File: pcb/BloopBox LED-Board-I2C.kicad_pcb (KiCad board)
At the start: 4 copper layers, 25 x 41.5 mm, 20 parts, among them J1 I2C, J2 V_BM, U1 IS31FL3199

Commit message: fix: add part numbers
Add missing LSCS Part numbers
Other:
- board text added: "BloopBox LED-Board I2C"
- board text removed: "BloopBox LED-Board"
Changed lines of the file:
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@@
     (descr "Capacitor SMD 0402 (1005 Metric), square (rectangular) end terminal, IPC_7351 nominal, (Body size source: IPC-SM-782 page 76, https://www.pcb-3d.com/wordpress/wp-content/uploads/ipc-sm-782a_amendment_1_and_2.pdf), generated with kicad-footprint-generator")
     (tags "capacitor")
+    (property "LCSC" "C52923")
     (property "Sheetfile" "BloopBox LED-Board-I2C.kicad_sch")
     (property "Sheetname" "")
@@
       (rotate (xyz 0 0 0))
     )
+    (model "${KICAD6_3DMODEL_DIR}/Package_DFN_QFN.3dshapes/QFN-20-1EP_3x3mm_P0.45mm_EP1.6x1.6mm.wrl"
+      (offset (xyz 0 0 0))
+      (scale (xyz 1 1 1))
+      (rotate (xyz 0 0 0))
+    )
   )
   (footprint "My_Footprints:JLCPCB_Tooling_Hole" (layer "F.Cu")
@@
     (descr "Capacitor SMD 0402 (1005 Metric), square (rectangular) end terminal, IPC_7351 nominal, (Body size source: IPC-SM-782 page 76, https://www.pcb-3d.com/wordpress/wp-content/uploads/ipc-sm-782a_amendment_1_and_2.pdf), generated with kicad-footprint-generator")
     (tags "capacitor")
+    (property "LCSC" "C1525")
     (property "Sheetfile" "BloopBox LED-Board-I2C.kicad_sch")
     (property "Sheetname" "")
@@
     (descr "Capacitor SMD 0402 (1005 Metric), square (rectangular) end terminal, IPC_7351 nominal, (Body size source: IPC-SM-782 page 76, https://www.pcb-3d.com/wordpress/wp-content/uploads/ipc-sm-782a_amendment_1_and_2.pdf), generated with kicad-footprint-generator")
     (tags "capacitor")
+    (property "LCSC" "C1525")
     (property "Sheetfile" "BloopBox LED-Board-I2C.kicad_sch")
     (property "Sheetname" "")
@@
     (descr "Resistor SMD 0402 (1005 Metric), square (rectangular) end terminal, IPC_7351 nominal, (Body size source: IPC-SM-782 page 72, https://www.pcb-3d.com/wordpress/wp-content/uploads/ipc-sm-782a_amendment_1_and_2.pdf), generated with kicad-footprint-generator")
     (tags "resistor")
+    (property "LCSC" "C25741")
     (property "Sheetfile" "BloopBox LED-Board-I2C.kicad_sch")
     (property "Sheetname" "")
@@
     (effects (font (size 1 1) (thickness 0.15)) (justify mirror))
   )
-  (gr_text "BloopBox\nLED-Board" (at 142.75 105.25) (layer "B.SilkS")
+  (gr_text "BloopBox\nLED-Board\nI2C" (at 142.75 107) (layer "B.SilkS")
     (effects (font (size 1.2 1.2) (thickness 0.2)) (justify mirror))
   )

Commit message: fix: add pin description
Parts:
- moved G*** 1.00 mm to (157.2, 106.0)
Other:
- board text added: "+"
- board text added: "-"
- board text added: "SCL"
- board text added: "SDA"
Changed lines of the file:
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@@
   )
   (footprint "My_Footprints:CutieMark5mmInverted" (layer "B.Cu")
-    (at 157.25 107 180)
+    (at 157.25 106 180)
     (attr board_only exclude_from_pos_files exclude_from_bom)
     (fp_text reference "G***" (at 0 0) (layer "B.SilkS") hide
@@
   (gr_line (start 137.5 85.5) (end 146.5 85.5) (layer "Edge.Cuts") (width 0.1))
   (gr_arc (start 142.5 115) (mid 138.964466 113.535534) (end 137.5 110) (layer "Edge.Cuts") (width 0.1))
-  (gr_text "qete.sh/el" (at 157.25 110.5) (layer "B.SilkS")
+  (gr_text "-" (at 153 111.75) (layer "B.SilkS")
+    (effects (font (size 1 1) (thickness 0.15)) (justify mirror))
+  )
+  (gr_text "qete.sh/el" (at 157.25 109.5) (layer "B.SilkS")
+    (effects (font (size 1 1) (thickness 0.15)) (justify mirror))
+  )
+  (gr_text "SDA" (at 149.25 111.75) (layer "B.SilkS")
+    (effects (font (size 1 0.75) (thickness 0.15)) (justify mirror))
+  )
+  (gr_text "+" (at 151 111.75) (layer "B.SilkS")
     (effects (font (size 1 1) (thickness 0.15)) (justify mirror))
   )
@@
     (effects (font (size 1.2 1.2) (thickness 0.2)) (justify mirror))
   )
+  (gr_text "SCL" (at 147 111.75) (layer "B.SilkS")
+    (effects (font (size 1 0.75) (thickness 0.15)) (justify mirror))
+  )
   (gr_text "JLCJLCJLCJLC" (at 158 121.25) (layer "F.SilkS")

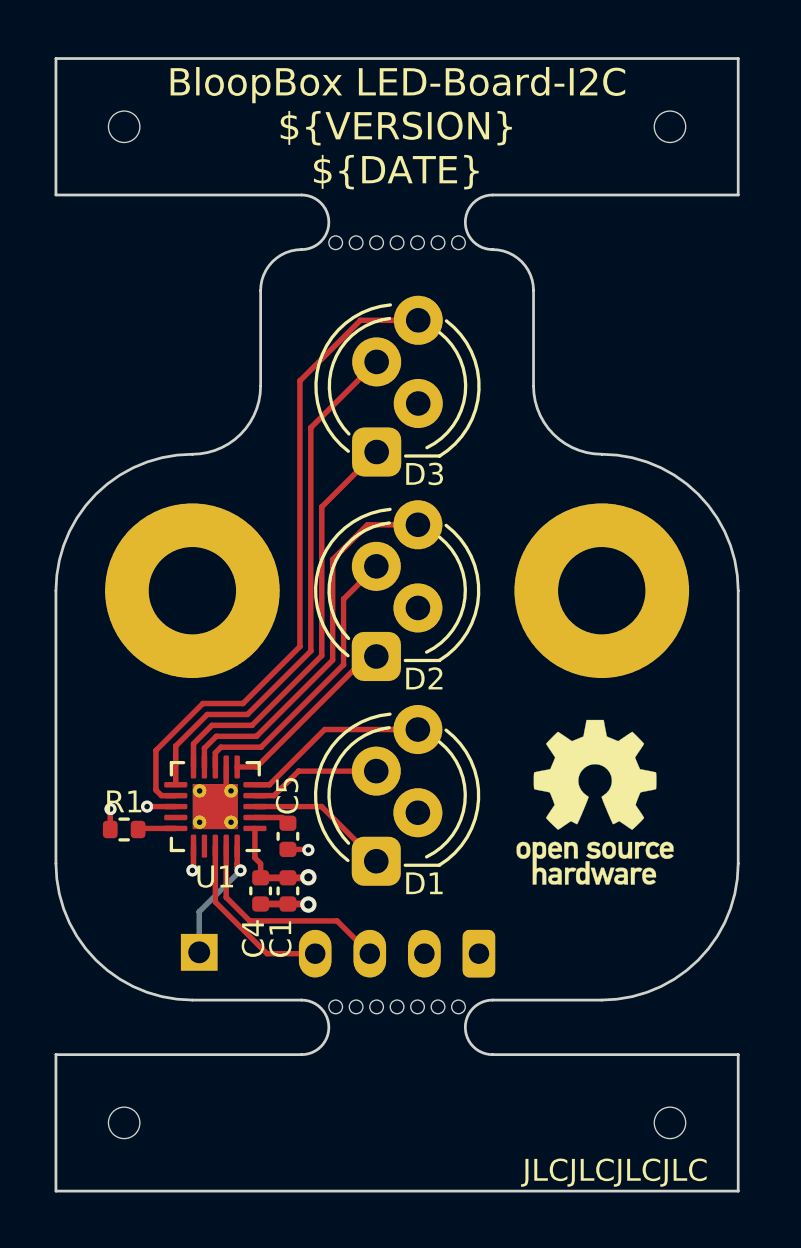
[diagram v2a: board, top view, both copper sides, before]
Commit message: feat: change LED controller to AW2013
replace the IS31FL3199 with AW2013 and remove additional LED footprints
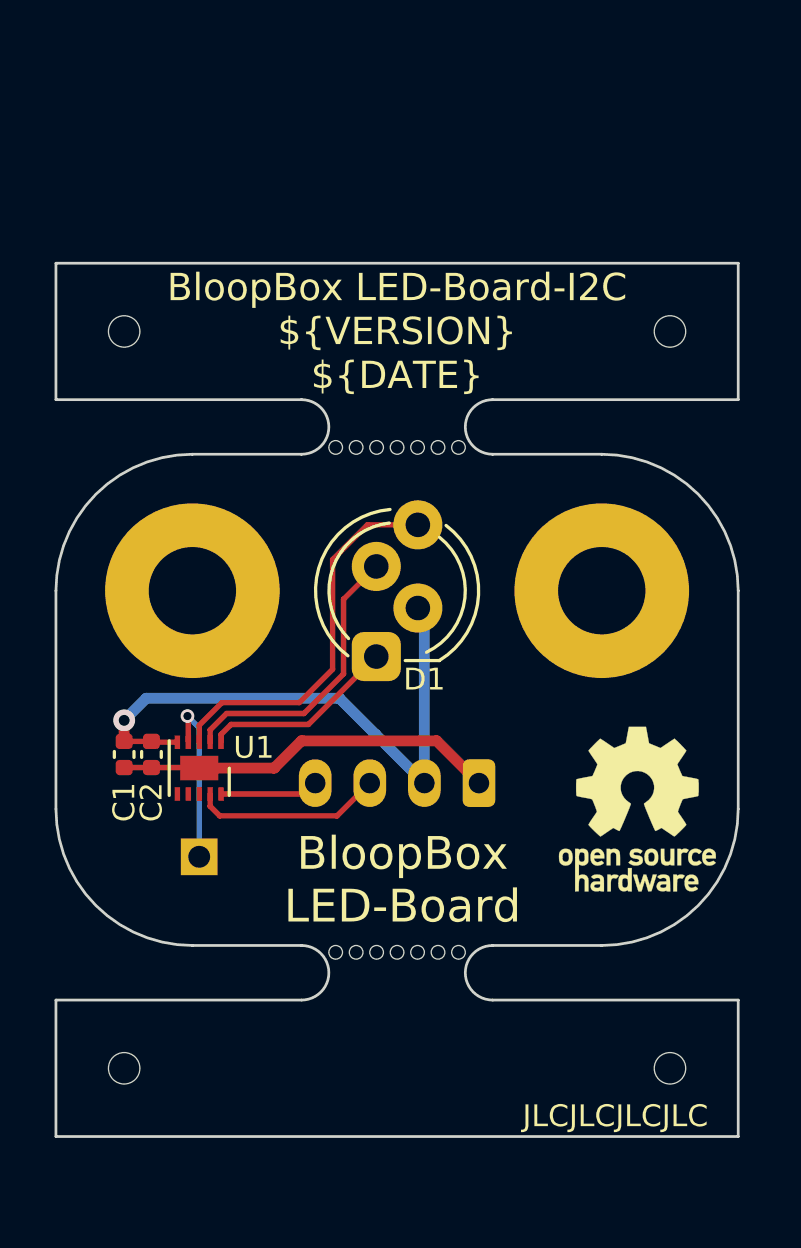
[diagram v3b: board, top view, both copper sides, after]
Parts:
- removed C5: 100n, Capacitor_SMD:C_0402_1005Metric
- removed D2, D3: LED_RAGB, LED_THT:LED_D5.0mm-4_RGB_Staggered_Pins
- removed R1: 100k, Resistor_SMD:R_0402_1005Metric
- J2: value V_BM -> INT
- U1: value IS31FL3199 -> AW2013DNR; footprint Package_DFN_QFN:QFN-20-1EP_3x3mm_P0.4mm_EP1.65x1.65mm_ThermalVias -> My_Footprints:DFN-10-1EP_2x2mm_P0.4mm_EP0.8x1.4
- moved C1 7.81 mm to (140.0, 106.0)
- moved D1 7.50 mm to (150.0, 100.0)
- moved REF** 7.50 mm to (160.0, 90.5)
- moved REF** 7.50 mm to (140.0, 90.5)
- moved mouse-bite-2mm-slot 7.50 mm to (150.0, 94.0)
- moved C2 6.40 mm to (141.0, 106.0)
- moved J1 6.25 mm to (153.0, 107.0)
- moved J2 3.50 mm to (142.8, 109.8)
- moved REF** 2.00 mm to (140.0, 117.5)
- moved REF** 2.00 mm to (160.0, 117.5)
- moved mouse-bite-2mm-slot 2.00 mm to (150.0, 114.0)
- moved G*** 1.60 mm to (158.5, 107.0)
- moved REF** 1.57 mm to (158.8, 108.0)
- moved U1 1.53 mm to (142.8, 106.5), turned to -90 degrees
- renumbered C4 to C2
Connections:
- D1 pad 1: /R1 -> /R
- D1 pad 3: /G1 -> /G
- D1 pad 4: /B1 -> /B
- J2 pad 1: /V_BM -> /~{INT}
- U1 pad 1: VCC -> /R
- U1 pad 10: /R3 -> /SCL
- U1 pad 11: /G3 -> GND
- U1 pad 2: /C_FILT -> /G
- U1 pad 3: /R1 -> /B
- U1 pad 4: /G1 -> /~{INT}
- U1 pad 5: /B1 -> VCC
- U1 pad 6: /R2 -> unconnected-(U1-Pad6)
- U1 pad 7: GND -> unconnected-(U1-Pad7)
- U1 pad 8: /G2 -> unconnected-(U1-Pad8)
- U1 pad 9: /B2 -> /SDA
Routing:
- net /B3: track 24.1 -> 0.00 mm
- net /G3: track 19.4 -> 0.00 mm
- net VCC: track 4.71 -> 21.9 mm, vias 2 -> 1
- net /R3: track 15.2 -> 0.00 mm
- net /B2: track 14.1 -> 0.00 mm
- net /B: track 0.00 -> 14.0 mm
- net /G2: track 10.7 -> 0.00 mm
- net /G: track 0.00 -> 10.6 mm
- net GND: track 5.79 -> 14.1 mm, vias 4 -> 0
- net /R: track 0.00 -> 7.15 mm
- net /B1: track 6.81 -> 0.00 mm
- net /R2: track 6.78 -> 0.00 mm
- net /~{INT}: track 0.00 -> 6.30 mm, vias 0 -> 1
- net /R1: track 5.28 -> 0.00 mm
- net /G1: track 4.82 -> 0.00 mm
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- removed copper zone on In1.Cu, net GND
- removed copper zone on In2.Cu, net VCC
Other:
- board size 25 x 41.5 mm -> 25 x 32 mm
- board text added: "BloopBox LED-Board"
- board text removed: "BloopBox LED-Board I2C"

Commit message: fix: remove unused inner layers
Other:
- copper layers 4 -> 2
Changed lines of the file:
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@@
   (layers
     (0 "F.Cu" signal)
-    (1 "In1.Cu" signal)
-    (2 "In2.Cu" signal)
     (31 "B.Cu" signal)
     (32 "B.Adhes" user "B.Adhesive")
@@
       (layer "F.Mask" (type "Top Solder Mask") (thickness 0.01))
       (layer "F.Cu" (type "copper") (thickness 0.035))
-      (layer "dielectric 1" (type "core") (thickness 0.48) (material "FR4") (epsilon_r 4.5) (loss_tangent 0.02))
-      (layer "In1.Cu" (type "copper") (thickness 0.035))
-      (layer "dielectric 2" (type "prepreg") (thickness 0.48) (material "FR4") (epsilon_r 4.5) (loss_tangent 0.02))
-      (layer "In2.Cu" (type "copper") (thickness 0.035))
-      (layer "dielectric 3" (type "core") (thickness 0.48) (material "FR4") (epsilon_r 4.5) (loss_tangent 0.02))
+      (layer "dielectric 1" (type "core") (thickness 1.51) (material "FR4") (epsilon_r 4.5) (loss_tangent 0.02))
       (layer "B.Cu" (type "copper") (thickness 0.035))
       (layer "B.Mask" (type "Bottom Solder Mask") (thickness 0.01))

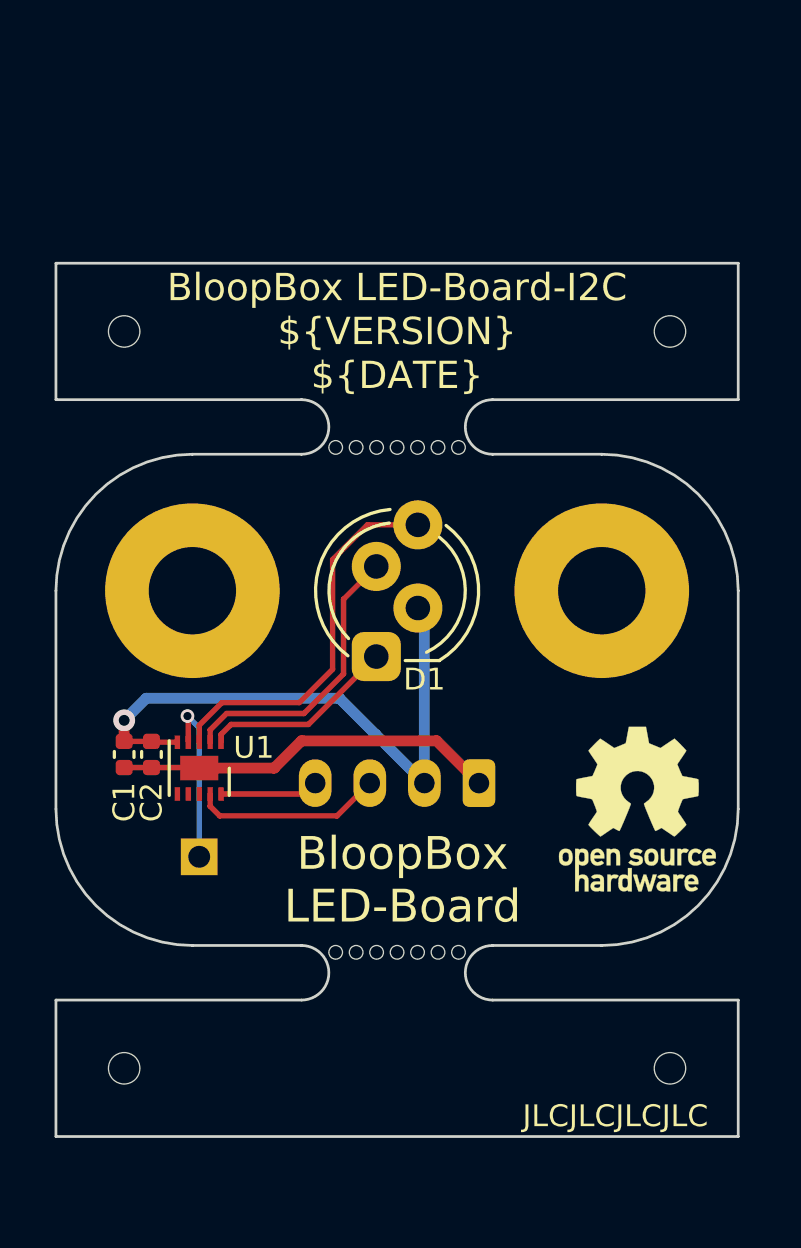
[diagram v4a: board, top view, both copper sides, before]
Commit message: feat: flip sides of LED and connector
Flip the LED to the bottom and the connector to the top to make it possible to have the connector assembled at the factory

Also updating sources to KiCad 8
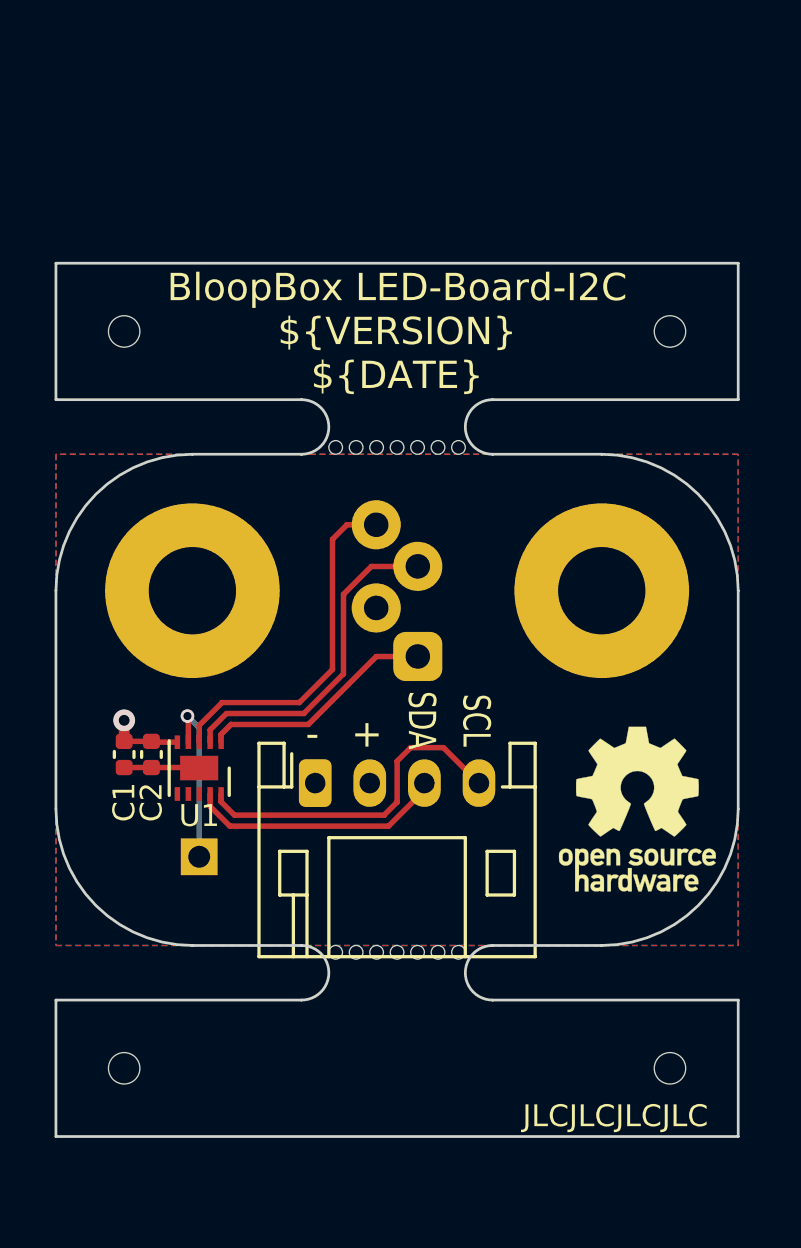
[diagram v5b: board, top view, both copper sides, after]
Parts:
- D1: moved to B.Cu
- J1: moved to F.Cu
- moved J1 6.00 mm to (147.0, 107.0), turned to 0 degrees
- moved D1 2.53 mm to (150.8, 102.4)
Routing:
- net VCC: track 21.9 -> 2.73 mm
- net GND: track 14.1 -> 2.76 mm
- net /SCL: track 3.62 -> 12.4 mm
- net /SDA: track 6.94 -> 9.41 mm
- net /G: track 10.6 -> 12.2 mm
- net /R: track 7.15 -> 8.68 mm
- net /B: track 14.0 -> 12.9 mm
- added copper zone on F.Cu, net GND
- added copper zone on B.Cu, net VCC
